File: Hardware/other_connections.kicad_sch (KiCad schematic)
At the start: 0 parts

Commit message: fcu, nu schematics, problem with pins
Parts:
- added R45, R46, R47, R48: 10, symbol Device:R
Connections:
- new net FCU_NU_GPIO1: R45.1
- new net FCU_NU_GPIO2: R46.1
- new net FCU_NU_GPIO3: R47.1
- new net FCU_NU_GPIO4: R48.1
- new net NU_FCU_GPIO1: R45.2
- new net NU_FCU_GPIO2: R46.2
- new net NU_FCU_GPIO3: R47.2
- new net NU_FCU_GPIO4: R48.2

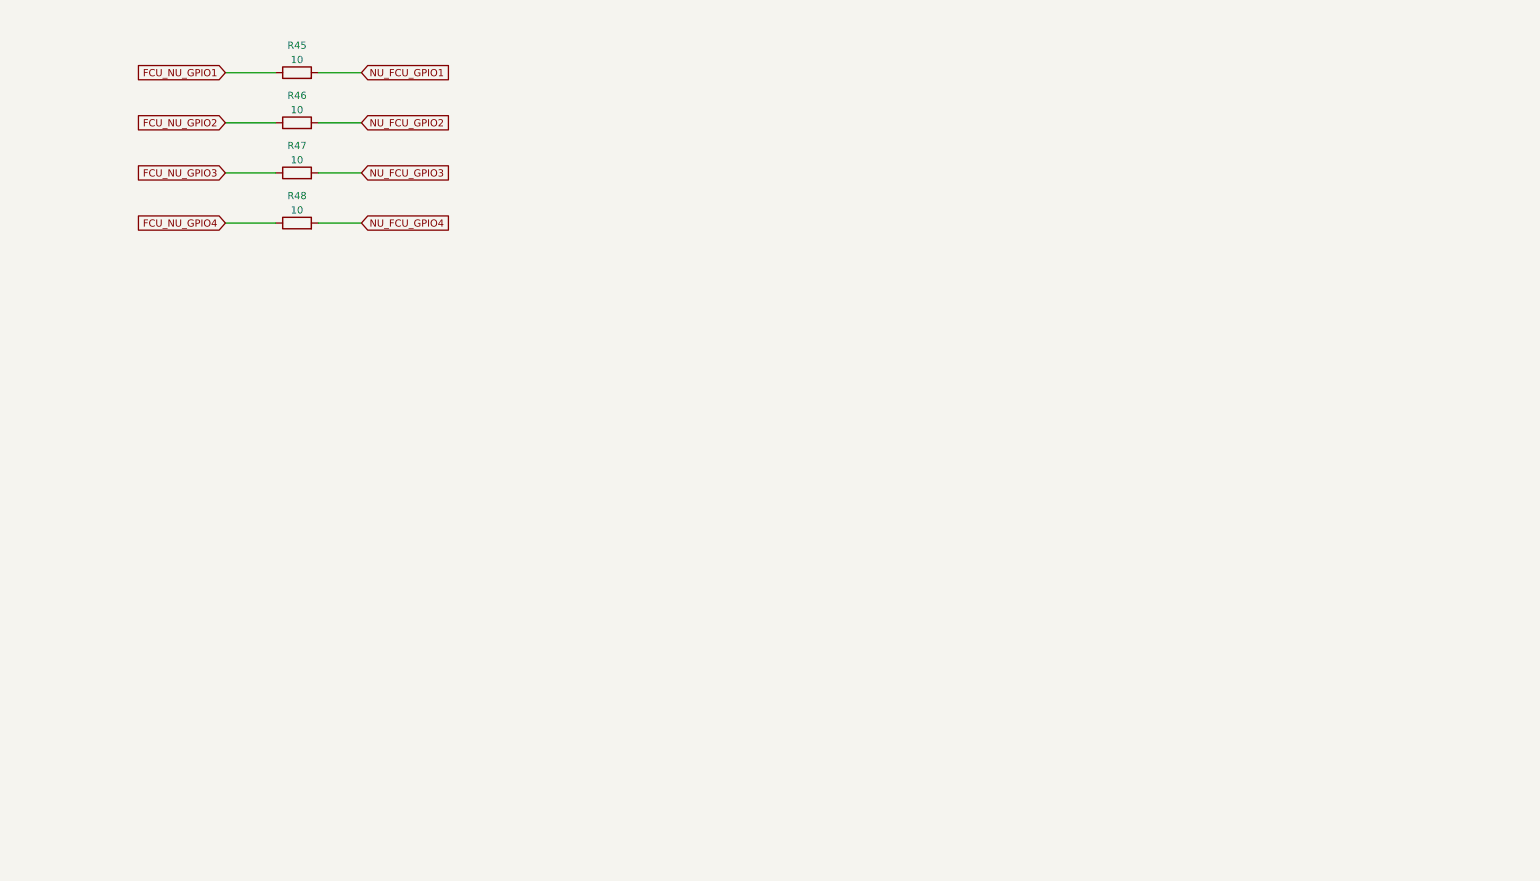
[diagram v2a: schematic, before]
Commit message: added projects, schematic almost done, need revision
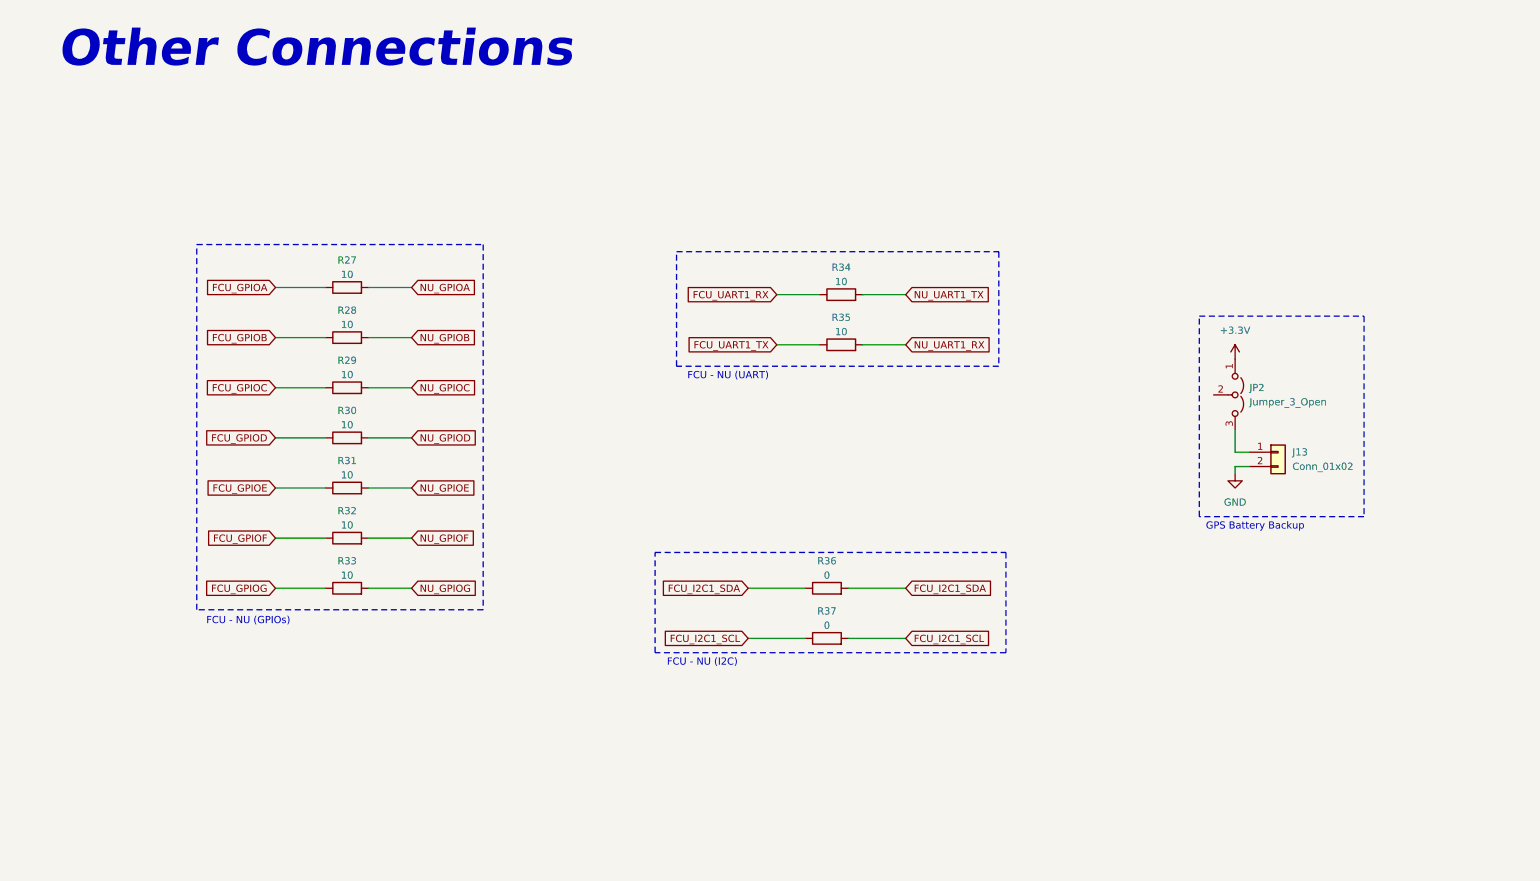
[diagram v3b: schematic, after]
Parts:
- added J13: Conn_01x02, symbol Connector_Generic:Conn_01x02
- added JP2: Jumper_3_Open, symbol Jumper:Jumper_3_Open
- added R31, R32, R33, R34, R35: 10, symbol Device:R
- added R36, R37: 0, symbol Device:R
- renumbered R45 to R27, R46 to R28, R47 to R29, R48 to R30
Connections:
- net FCU_NU_GPIO1 renamed FCU_GPIOA
- net FCU_NU_GPIO2 renamed FCU_GPIOB
- net FCU_NU_GPIO3 renamed FCU_GPIOC
- net FCU_NU_GPIO4 renamed FCU_GPIOD
- net NU_FCU_GPIO1 renamed NU_GPIOA
- net NU_FCU_GPIO2 renamed NU_GPIOB
- net NU_FCU_GPIO3 renamed NU_GPIOC
- net NU_FCU_GPIO4 renamed NU_GPIOD
- new net: J13.1 (Pin_1), JP2.3 (B)
- new net +3.3V: JP2.1 (A)
- new net FCU_GPIOE: R31.1
- new net FCU_GPIOF: R32.1
- new net FCU_GPIOG: R33.1
- new net FCU_I2C1_SCL: R37.1, R37.2
- new net FCU_I2C1_SDA: R36.1, R36.2
- new net FCU_UART1_RX: R34.1
- new net FCU_UART1_TX: R35.1
- new net GND: J13.2 (Pin_2)
- new net NU_GPIOE: R31.2
- new net NU_GPIOF: R32.2
- new net NU_GPIOG: R33.2
- new net NU_UART1_RX: R35.2
- new net NU_UART1_TX: R34.2
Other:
- note added: "FCU - NU (GPIOs)"
- note added: "FCU - NU (I2C)"
- note added: "FCU - NU (UART)"
- note added: "GPS Battery Backup"
- note added: "Other Connections"
- moved on the sheet: R27, R28, R29, R30

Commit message: version 0.1.0
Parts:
- added C60, C61, C62, C63: 100n, symbol Device:C
- added D12, D14: SD103AWS, symbol Device:D_Schottky
- added D13, D15: G, symbol Device:LED
- added FB3, FB4: FerriteBead, symbol Device:FerriteBead
- added J14, J15: Conn_02x05_Odd_Even, symbol Connector_Generic:Conn_02x05_Odd_Even
- added J16, J17: USB_B_Micro, symbol Connector:USB_B_Micro
- added R50, R51: 560, symbol Device:R
- added U16, U17: CH330N, Package_SO:SOIC-8_3.9x4.9mm_P1.27mm, symbol Interface_USB:CH330N
- renumbered R27 to R39, R28 to R40, R29 to R41, R30 to R42, R31 to R43, R32 to R44, R33 to R45, R36 to R46, R37 to R47, R34 to R48, R35 to R49
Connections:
- net +3.3V: now also JP2.3 (B), J14.7 (Pin_7), J14.8 (Pin_8), J15.7 (Pin_7), J15.8 (Pin_8); no longer JP2.1 (A)
- net FCU_I2C1_SCL: no longer R47.2
- net FCU_I2C1_SDA: no longer R46.2
- net GND: now also C60.2, C61.2, C62.2, C63.2, J14.3 (Pin_3), J14.4 (Pin_4), J15.3 (Pin_3), J15.4 (Pin_4), J16.5 (GND), J16.6 (Shield), J17.5 (GND), J17.6 (Shield), R50.2, R51.2, U16.3 (GND), U17.3 (GND)
- net GPS_BACKUP_BAT: now reaches JP2.2 (C)
- net at J13.1 (Pin_1): now also JP2.1 (A); no longer JP2.3 (B)
- new net: C63.1, D14.2 (A), D15.2 (A), J17.1 (VBUS), U17.5 (VCC)
- new net: J17.2 (D-), U17.2 (UD-)
- new net: J17.3 (D+), U17.1 (UD+)
- new net: C62.1, U17.8 (V3)
- new net: D12.1 (K), FB3.1
- new net: C61.1, D12.2 (A), D13.2 (A), J16.1 (VBUS), U16.5 (VCC)
- new net: D13.1 (K), R50.1
- new net: C60.1, U16.8 (V3)
- new net: D14.1 (K), FB4.1
- new net: D15.1 (K), R51.1
- new net: J16.3 (D+), U16.1 (UD+)
- new net: J16.2 (D-), U16.2 (UD-)
- new net +5V: FB3.2, FB4.2
- new net FCU_NRST: J14.1 (Pin_1)
- new net FCU_SWCLK: J14.6 (Pin_6)
- new net FCU_SWDIO: J14.2 (Pin_2)
- new net FCU_UART2_RX: U16.6 (TXD)
- new net FCU_UART2_TX: U16.7 (RXD)
- new net NU_I2C2_SCL: R47.2
- new net NU_I2C2_SDA: R46.2
- new net NU_NRST: J15.1 (Pin_1)
- new net NU_SWCLK: J15.6 (Pin_6)
- new net NU_SWDIO: J15.2 (Pin_2)
- new net NU_UART2_RX: U17.6 (TXD)
- new net NU_UART2_TX: U17.7 (RXD)
- no-connect marks 0 -> 10
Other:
- note added: "Logging Debug USBs"
- note added: "Serial Wire Debug Connectors"
- note added: "These connections was based on China ST-Link version"
- company: (none) -> Breno Soares Alves
- title: (none) -> Other Connections
- moved on the sheet: J13, JP2, R39, R40, R41, R42, R43, R44, R45, R46, R47, R48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

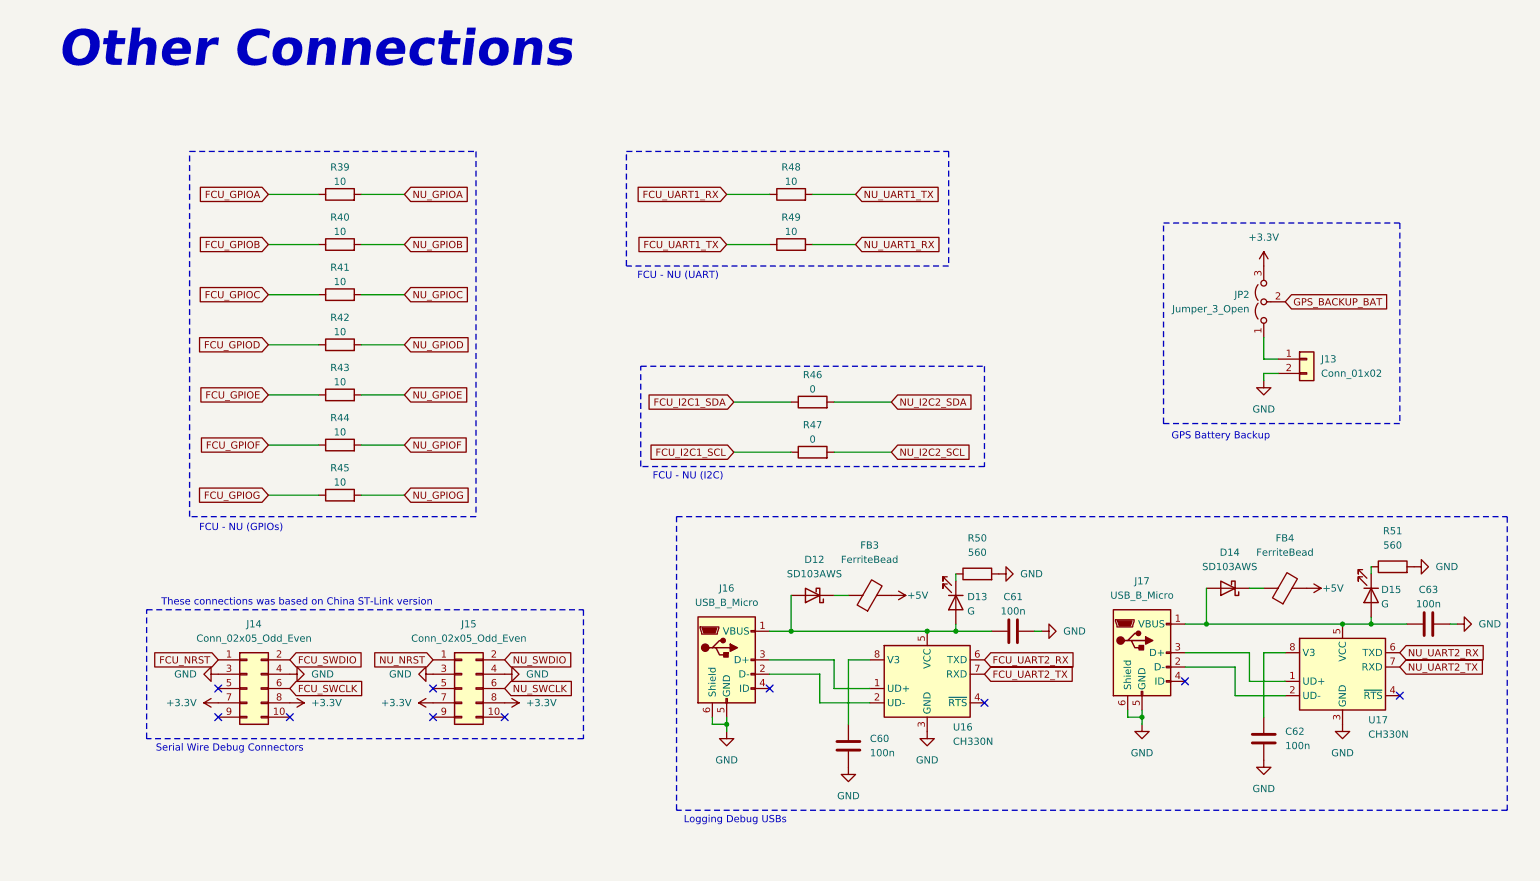
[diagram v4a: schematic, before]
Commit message: version 0.1.1, added dfu usb to firmware upload, changed pwm channels
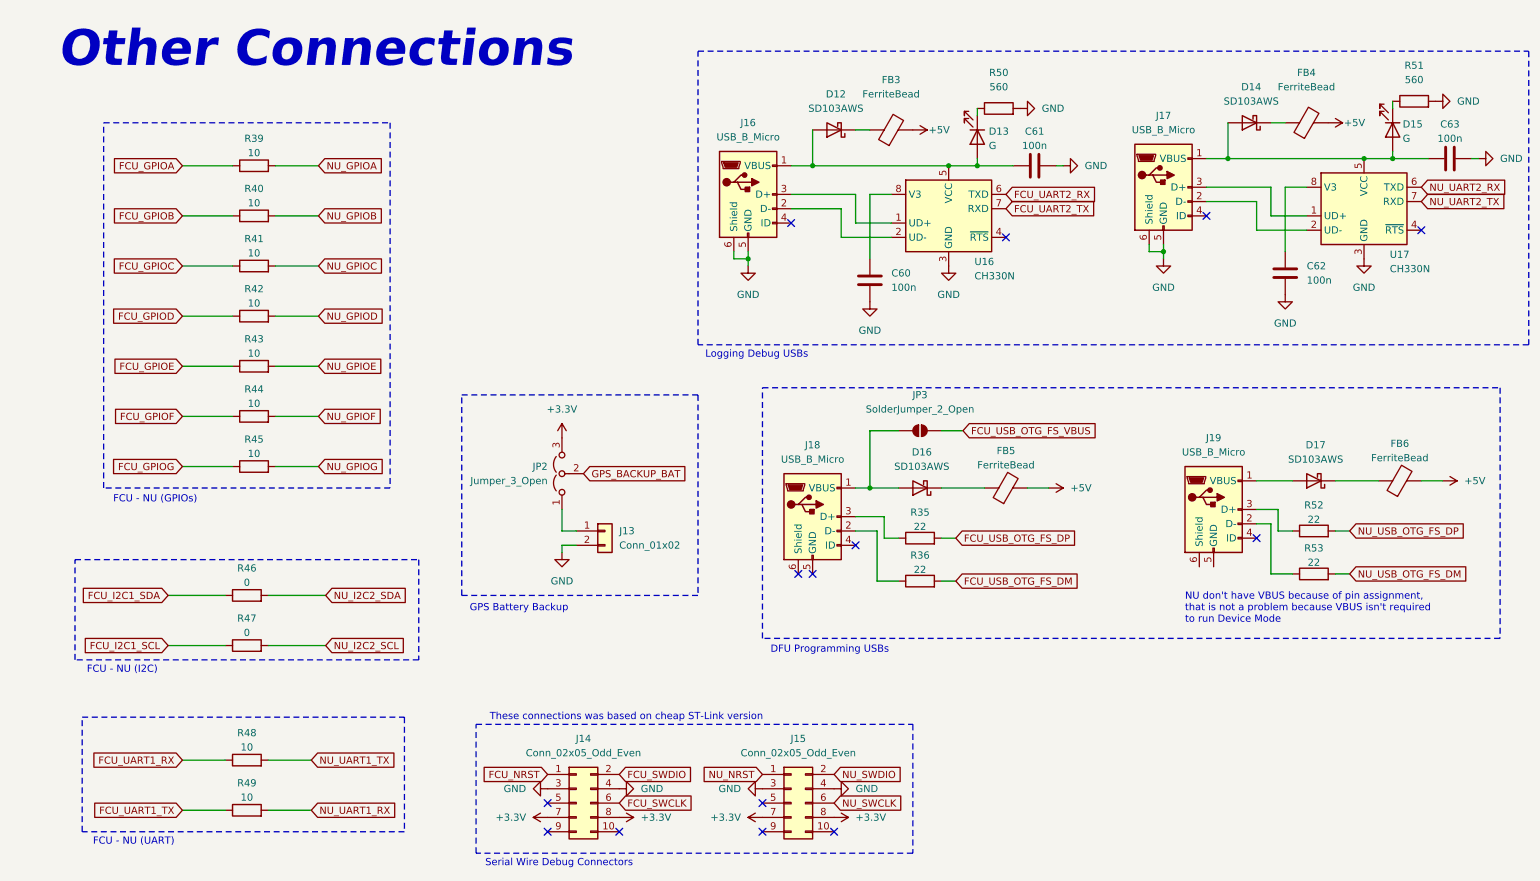
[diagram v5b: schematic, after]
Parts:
- added D16, D17: SD103AWS, symbol Device:D_Schottky
- added FB5, FB6: FerriteBead, symbol Device:FerriteBead
- added J18, J19: USB_B_Micro, symbol Connector:USB_B_Micro
- added JP3: SolderJumper_2_Open, symbol Jumper:SolderJumper_2_Open
- added R35, R36, R52, R53: 22, symbol Device:R
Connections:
- net +5V: now also FB5.2, FB6.2
- new net: J18.2 (D-), R36.1
- new net: D17.1 (K), FB6.1
- new net: D17.2 (A), J19.1 (VBUS)
- new net: D16.2 (A), J18.1 (VBUS), JP3.1 (A)
- new net: D16.1 (K), FB5.1
- new net: J19.3 (D+), R52.1
- new net: J19.2 (D-), R53.1
- new net: J18.3 (D+), R35.1
- new net FCU_USB_OTG_FS_DM: R36.2
- new net FCU_USB_OTG_FS_DP: R35.2
- new net FCU_USB_OTG_FS_VBUS: JP3.2 (B)
- new net NU_USB_OTG_FS_DM: R53.2
- new net NU_USB_OTG_FS_DP: R52.2
- no-connect marks 10 -> 14
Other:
- note added: "DFU Programming USBs"
- note added: "NU don't have VBUS because of pin assignment, that is not a problem because VBUS isn't required to run Device Mode"
- note added: "These connections was based on cheap ST-Link version"
- note removed: "These connections was based on China ST-Link version"
- moved on the sheet: C60, C61, C62, C63, D12, D13, D14, D15, FB3, FB4, J13, J14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
